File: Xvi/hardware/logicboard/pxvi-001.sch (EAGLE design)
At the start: 90 parts, among them J1 MKR, J4 QWIIC_RIGHT_ANGLE, J5 SPI, J6 QWIIC_RIGHT_ANGLE, J7 DIN5, K1 G5V1, Q1 60V/32A/35mΩ, Q10 60V/32A/35mΩ, Q11 60V/32A/35mΩ, Q12 60V/32A/35mΩ, Q13 60V/32A/35mΩ, Q14 60V/32A/35mΩ, Q15 60V/32A/35mΩ, Q16 60V/32A/35mΩ, Q2 60V/32A/35mΩ, Q3 60V/32A/35mΩ, Q4 60V/32A/35mΩ, Q5 60V/32A/35mΩ, Q6 60V/32A/35mΩ, Q7 60V/32A/35mΩ, Q8 60V/32A/35mΩ, Q9 60V/32A/35mΩ, T1 2SC1815, U1 DS18B20, X1 ADAFRUIT-PCA9685, X2 MKDSN1,5/2-5,08

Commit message: Wired.
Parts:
- added C25: 10n, resistor:C-EU025-024X044
- added D2: DIODE-1N4148, SparkFun-DiscreteSemi:DIODE-1N4148
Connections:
- net N$1: now also C25.2, D2.A
- net VCC: now also C25.1, D2.C
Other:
- moved on the sheet: K1, R2, R3
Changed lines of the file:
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@@
 <part name="SUPPLY62" library="supply2" library_urn="urn:adsk.eagle:library:372" deviceset="VCC" device=""/>
 <part name="P+20" library="supply1" library_urn="urn:adsk.eagle:library:371" deviceset="V+" device=""/>
+<part name="C25" library="resistor" library_urn="urn:adsk.eagle:library:348" deviceset="C-EU" device="025-024X044" package3d_urn="urn:adsk.eagle:package:23630/1" value="10n"/>
+<part name="D2" library="SparkFun-DiscreteSemi" library_urn="urn:adsk.eagle:library:514" deviceset="DIODE" device="-1N4148" package3d_urn="urn:adsk.eagle:package:38452/1" value=""/>
 </parts>
 <sheets>
@@
 <wire x1="360.68" y1="121.92" x2="304.8" y2="121.92" width="0.1524" layer="94" style="shortdash"/>
 <wire x1="218.44" y1="254" x2="218.44" y2="167.64" width="0.1524" layer="94" style="shortdash"/>
-<wire x1="218.44" y1="167.64" x2="335.28" y2="167.64" width="0.1524" layer="94" style="shortdash"/>
 <wire x1="335.28" y1="254" x2="218.44" y2="254" width="0.1524" layer="94" style="shortdash"/>
 </plain>
@@
 <attribute name="VALUE" x="327.66" y="157.48" size="1.778" layer="96"/>
 </instance>
-<instance part="K1" gate="1" x="340.36" y="165.1" smashed="yes">
-<attribute name="VALUE" x="341.63" y="168.021" size="1.778" layer="96"/>
-<attribute name="PART" x="341.63" y="170.18" size="1.778" layer="95"/>
+<instance part="K1" gate="1" x="340.36" y="170.18" smashed="yes">
+<attribute name="VALUE" x="341.63" y="173.101" size="1.778" layer="96"/>
+<attribute name="PART" x="341.63" y="175.26" size="1.778" layer="95"/>
 </instance>
 <instance part="K1" gate="2" x="358.14" y="162.56" smashed="yes">
@@
 </instance>
 <instance part="SUPPLY36" gate="GND" x="264.16" y="198.12" smashed="yes"/>
-<instance part="R2" gate="G$1" x="325.12" y="152.4" smashed="yes">
-<attribute name="NAME" x="325.12" y="154.94" size="1.778" layer="95" align="center"/>
-<attribute name="VALUE" x="330.2" y="154.94" size="1.778" layer="96" align="center"/>
-</instance>
-<instance part="R3" gate="G$1" x="332.74" y="139.7" smashed="yes" rot="R90">
-<attribute name="NAME" x="330.2" y="139.7" size="1.778" layer="95" rot="R90" align="center"/>
-<attribute name="VALUE" x="330.2" y="144.78" size="1.778" layer="96" rot="R90" align="center"/>
-</instance>
-<instance part="SUPPLY37" gate="GND" x="332.74" y="129.54" smashed="yes"/>
+<instance part="R2" gate="G$1" x="312.42" y="152.4" smashed="yes">
+<attribute name="NAME" x="312.42" y="154.94" size="1.778" layer="95" align="center"/>
+<attribute name="VALUE" x="317.5" y="154.94" size="1.778" layer="96" align="center"/>
+</instance>
+<instance part="R3" gate="G$1" x="320.04" y="142.24" smashed="yes" rot="R90">
+<attribute name="NAME" x="317.5" y="142.24" size="1.778" layer="95" rot="R90" align="center"/>
+<attribute name="VALUE" x="317.5" y="147.32" size="1.778" layer="96" rot="R90" align="center"/>
+</instance>
+<instance part="SUPPLY37" gate="GND" x="320.04" y="129.54" smashed="yes"/>
 <instance part="SUPPLY38" gate="G$1" x="373.38" y="182.88" smashed="yes">
 <attribute name="VALUE" x="373.38" y="187.96" size="1.778" layer="96" align="bottom-center"/>
@@
 <instance part="P+20" gate="1" x="274.32" y="236.22" smashed="yes">
 <attribute name="VALUE" x="274.32" y="238.76" size="1.778" layer="96"/>
+</instance>
+<instance part="C25" gate="G$1" x="325.12" y="170.18" smashed="yes">
+<attribute name="NAME" x="322.58" y="170.18" size="1.778" layer="95" align="bottom-center"/>
+<attribute name="VALUE" x="322.58" y="165.1" size="1.778" layer="96" align="bottom-center"/>
+</instance>
+<instance part="D2" gate="G$1" x="332.74" y="170.18" smashed="yes" rot="R90">
+<attribute name="NAME" x="337.82" y="170.18" size="1.778" layer="95" rot="R270" align="bottom-center"/>
+<attribute name="VALUE" x="334.772" y="167.64" size="1.778" layer="96" font="vector" rot="R90" align="top-left"/>
 </instance>
 </instances>
@@
 <segment>
 <pinref part="R3" gate="G$1" pin="1"/>
-<wire x1="332.74" y1="134.62" x2="332.74" y2="132.08" width="0.1524" layer="91"/>
+<wire x1="320.04" y1="137.16" x2="320.04" y2="132.08" width="0.1524" layer="91"/>
 <pinref part="SUPPLY37" gate="GND" pin="GND"/>
 </segment>
@@
 <pinref part="SUPPLY34" gate="G$1" pin="VCC"/>
 <pinref part="K1" gate="1" pin="1"/>
-<wire x1="340.36" y1="180.34" x2="340.36" y2="170.18" width="0.1524" layer="91"/>
+<wire x1="340.36" y1="180.34" x2="340.36" y2="177.8" width="0.1524" layer="91"/>
+<wire x1="340.36" y1="177.8" x2="340.36" y2="175.26" width="0.1524" layer="91"/>
+<wire x1="340.36" y1="177.8" x2="332.74" y2="177.8" width="0.1524" layer="91"/>
+<junction x="340.36" y="177.8"/>
+<pinref part="C25" gate="G$1" pin="1"/>
+<wire x1="332.74" y1="177.8" x2="325.12" y2="177.8" width="0.1524" layer="91"/>
+<wire x1="325.12" y1="177.8" x2="325.12" y2="172.72" width="0.1524" layer="91"/>
+<pinref part="D2" gate="G$1" pin="C"/>
+<wire x1="332.74" y1="172.72" x2="332.74" y2="177.8" width="0.1524" layer="91"/>
+<junction x="332.74" y="177.8"/>
 </segment>
 <segment>
@@
 <segment>
 <pinref part="R2" gate="G$1" pin="1"/>
-<wire x1="320.04" y1="152.4" x2="317.5" y2="152.4" width="0.1524" layer="91"/>
-<label x="317.5" y="152.4" size="0.8128" layer="95" rot="R180" xref="yes"/>
+<wire x1="307.34" y1="152.4" x2="304.8" y2="152.4" width="0.1524" layer="91"/>
+<label x="304.8" y="152.4" size="0.8128" layer="95" rot="R180" xref="yes"/>
 </segment>
 </net>
@@
 <pinref part="K1" gate="1" pin="2"/>
 <pinref part="T1" gate="G$1" pin="C"/>
-<wire x1="340.36" y1="160.02" x2="340.36" y2="157.48" width="0.1524" layer="91"/>
+<wire x1="340.36" y1="165.1" x2="340.36" y2="162.56" width="0.1524" layer="91"/>
+<pinref part="D2" gate="G$1" pin="A"/>
+<wire x1="340.36" y1="162.56" x2="340.36" y2="157.48" width="0.1524" layer="91"/>
+<wire x1="332.74" y1="167.64" x2="332.74" y2="162.56" width="0.1524" layer="91"/>
+<wire x1="332.74" y1="162.56" x2="340.36" y2="162.56" width="0.1524" layer="91"/>
+<junction x="340.36" y="162.56"/>
+<wire x1="332.74" y1="162.56" x2="325.12" y2="162.56" width="0.1524" layer="91"/>
+<junction x="332.74" y="162.56"/>
+<pinref part="C25" gate="G$1" pin="2"/>
+<wire x1="325.12" y1="162.56" x2="325.12" y2="165.1" width="0.1524" layer="91"/>
 </segment>
 </net>
@@
 <segment>
 <pinref part="T1" gate="G$1" pin="B"/>
-<wire x1="335.28" y1="152.4" x2="332.74" y2="152.4" width="0.1524" layer="91"/>
+<wire x1="335.28" y1="152.4" x2="320.04" y2="152.4" width="0.1524" layer="91"/>
 <pinref part="R2" gate="G$1" pin="2"/>
 <pinref part="R3" gate="G$1" pin="2"/>
-<wire x1="332.74" y1="152.4" x2="330.2" y2="152.4" width="0.1524" layer="91"/>
-<wire x1="332.74" y1="152.4" x2="332.74" y2="144.78" width="0.1524" layer="91"/>
-<junction x="332.74" y="152.4"/>
-</segment>
-</net>
+<wire x1="320.04" y1="152.4" x2="317.5" y2="152.4" width="0.1524" layer="91"/>
+<wire x1="320.04" y1="152.4" x2="320.04" y2="147.32" width="0.1524" layer="91"/>
+<junction x="320.04" y="152.4"/>
+</segment>
+</net>

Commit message: Wired.
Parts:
- removed J4, J6: QWIIC_RIGHT_ANGLE, SparkFun-Connectors:QWIIC_CONNECTORJS-1MM
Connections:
- net GND: no longer J4.1, J6.1
- net SCL: no longer J4.4, J6.4
- net SDA: no longer J4.3, J6.3
- net VCC: no longer J4.2, J6.2
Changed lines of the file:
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@@
 <part name="SUPPLY38" library="supply2" library_urn="urn:adsk.eagle:library:372" deviceset="VCC" device=""/>
 <part name="SUPPLY39" library="supply2" deviceset="GND" device=""/>
-<part name="J4" library="SparkFun-Connectors" library_urn="urn:adsk.eagle:library:513" deviceset="QWIIC_CONNECTOR" device="JS-1MM" package3d_urn="urn:adsk.eagle:package:41390393/1" value="QWIIC_RIGHT_ANGLE"/>
-<part name="J6" library="SparkFun-Connectors" library_urn="urn:adsk.eagle:library:513" deviceset="QWIIC_CONNECTOR" device="JS-1MM" package3d_urn="urn:adsk.eagle:package:41390393/1" value="QWIIC_RIGHT_ANGLE"/>
 <part name="SUPPLY40" library="supply2" library_urn="urn:adsk.eagle:library:372" deviceset="VCC" device=""/>
 <part name="SUPPLY41" library="supply2" deviceset="GND" device=""/>
@@
 </instance>
 <instance part="SUPPLY39" gate="GND" x="350.52" y="129.54" smashed="yes"/>
-<instance part="J4" gate="J1" x="215.9" y="139.7" smashed="yes">
-<attribute name="VALUE" x="210.82" y="134.366" size="1.778" layer="96" font="vector" align="top-left"/>
-<attribute name="NAME" x="210.82" y="147.574" size="1.778" layer="95" font="vector"/>
-</instance>
-<instance part="J6" gate="J1" x="215.9" y="116.84" smashed="yes">
-<attribute name="VALUE" x="210.82" y="111.506" size="1.778" layer="96" font="vector" align="top-left"/>
-<attribute name="NAME" x="210.82" y="124.714" size="1.778" layer="95" font="vector"/>
-</instance>
 <instance part="SUPPLY40" gate="G$1" x="246.38" y="149.86" smashed="yes">
 <attribute name="VALUE" x="246.38" y="154.94" size="1.778" layer="96" align="bottom-center"/>
@@
 </segment>
 <segment>
-<pinref part="J4" gate="J1" pin="1"/>
 <wire x1="223.52" y1="137.16" x2="233.68" y2="137.16" width="0.1524" layer="91"/>
 <wire x1="233.68" y1="137.16" x2="246.38" y2="137.16" width="0.1524" layer="91"/>
 <wire x1="246.38" y1="137.16" x2="246.38" y2="134.62" width="0.1524" layer="91"/>
-<pinref part="J6" gate="J1" pin="1"/>
 <wire x1="223.52" y1="114.3" x2="233.68" y2="114.3" width="0.1524" layer="91"/>
 <wire x1="233.68" y1="114.3" x2="233.68" y2="137.16" width="0.1524" layer="91"/>
@@
 </segment>
 <segment>
-<pinref part="J4" gate="J1" pin="2"/>
 <wire x1="223.52" y1="139.7" x2="231.14" y2="139.7" width="0.1524" layer="91"/>
-<pinref part="J6" gate="J1" pin="2"/>
 <wire x1="223.52" y1="116.84" x2="231.14" y2="116.84" width="0.1524" layer="91"/>
 <wire x1="231.14" y1="116.84" x2="231.14" y2="139.7" width="0.1524" layer="91"/>
@@
 </segment>
 <segment>
-<pinref part="J4" gate="J1" pin="3"/>
 <wire x1="223.52" y1="142.24" x2="228.6" y2="142.24" width="0.1524" layer="91"/>
-<pinref part="J6" gate="J1" pin="3"/>
 <wire x1="228.6" y1="142.24" x2="238.76" y2="142.24" width="0.1524" layer="91"/>
 <wire x1="228.6" y1="142.24" x2="228.6" y2="119.38" width="0.1524" layer="91"/>
@@
 </segment>
 <segment>
-<pinref part="J4" gate="J1" pin="4"/>
 <wire x1="223.52" y1="144.78" x2="226.06" y2="144.78" width="0.1524" layer="91"/>
-<pinref part="J6" gate="J1" pin="4"/>
 <wire x1="226.06" y1="144.78" x2="238.76" y2="144.78" width="0.1524" layer="91"/>
 <wire x1="223.52" y1="121.92" x2="226.06" y2="121.92" width="0.1524" layer="91"/>

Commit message: Re-routed.
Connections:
- net N$1 renamed VRLY
- net N$4 renamed FAN
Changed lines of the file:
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@@
 </segment>
 </net>
-<net name="N$1" class="0">
+<net name="VRLY" class="2">
 <segment>
 <pinref part="K1" gate="1" pin="2"/>
@@
 </segment>
 </net>
-<net name="N$4" class="0">
+<net name="FAN" class="2">
 <segment>
 <pinref part="X2" gate="-2" pin="KL"/>

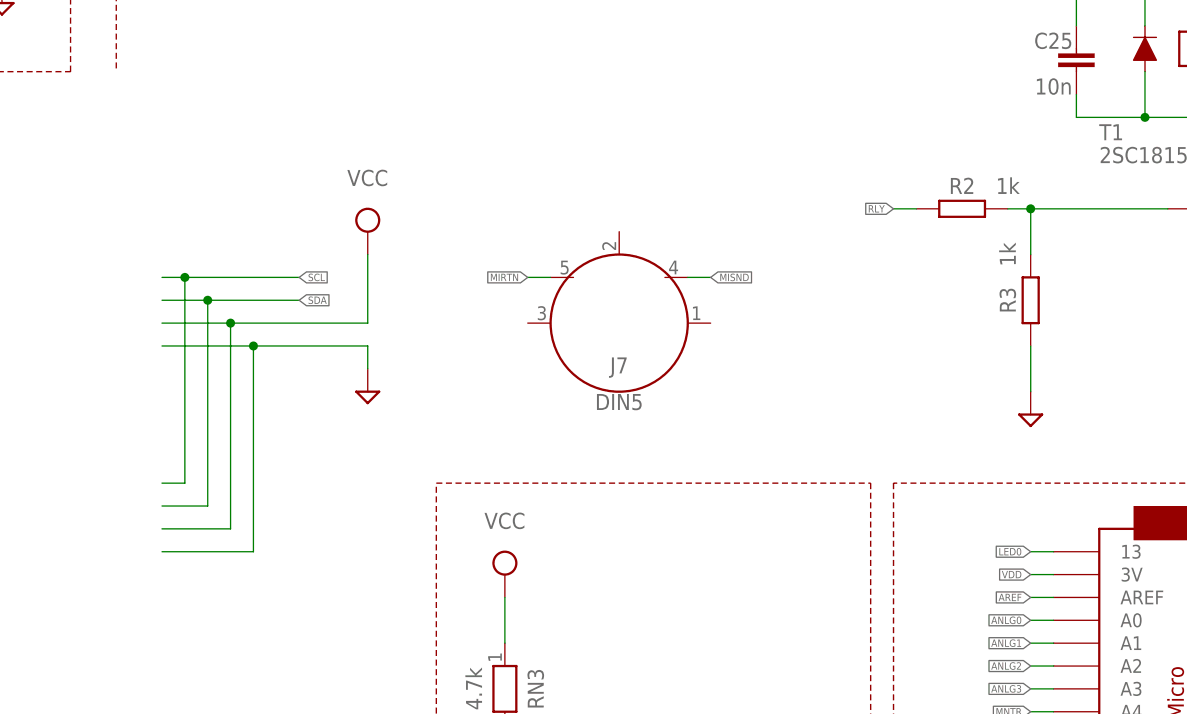
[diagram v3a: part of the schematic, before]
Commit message: GND pattern.
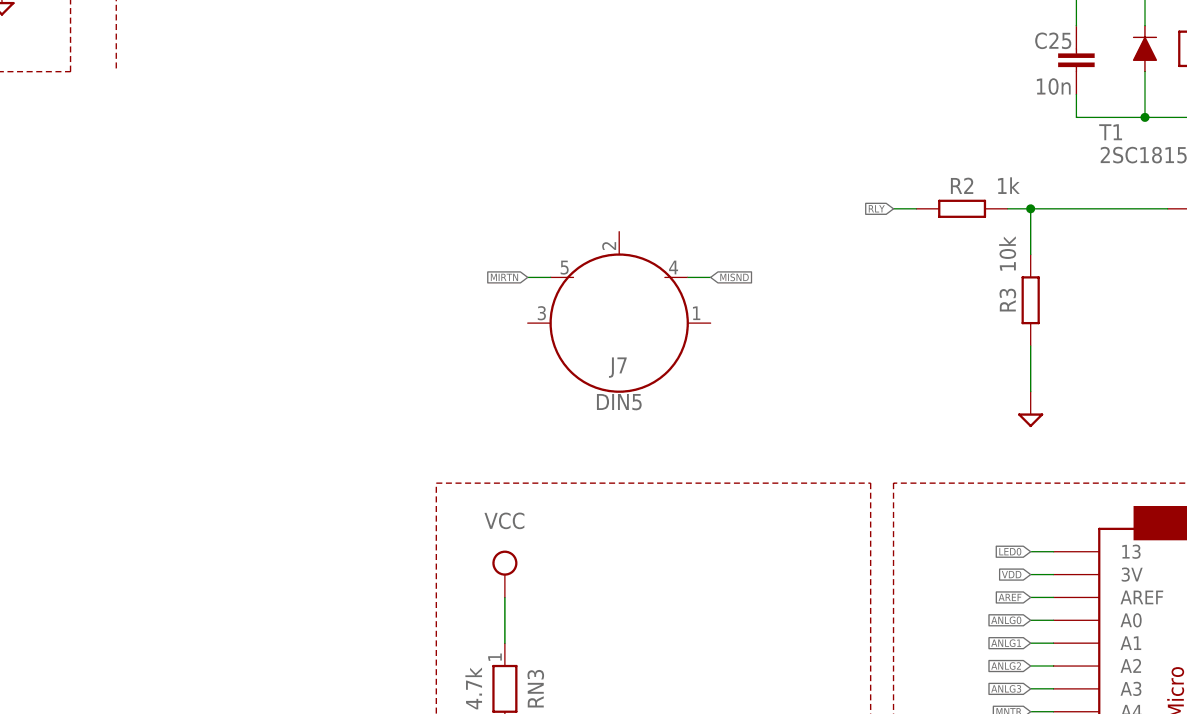
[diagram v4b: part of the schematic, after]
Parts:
- R3: value 1k -> 10k
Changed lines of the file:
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@@
 <part name="SUPPLY36" library="supply2" deviceset="GND" device=""/>
 <part name="R2" library="resistor" library_urn="urn:adsk.eagle:library:348" deviceset="R-EU_" device="0204/5" package3d_urn="urn:adsk.eagle:package:23488/1" value="1k"/>
-<part name="R3" library="resistor" library_urn="urn:adsk.eagle:library:348" deviceset="R-EU_" device="0204/5" package3d_urn="urn:adsk.eagle:package:23488/1" value="1k"/>
+<part name="R3" library="resistor" library_urn="urn:adsk.eagle:library:348" deviceset="R-EU_" device="0204/5" package3d_urn="urn:adsk.eagle:package:23488/1" value="10k"/>
 <part name="SUPPLY37" library="supply2" deviceset="GND" device=""/>
 <part name="SUPPLY38" library="supply2" library_urn="urn:adsk.eagle:library:372" deviceset="VCC" device=""/>
 <part name="SUPPLY39" library="supply2" deviceset="GND" device=""/>
-<part name="SUPPLY40" library="supply2" library_urn="urn:adsk.eagle:library:372" deviceset="VCC" device=""/>
-<part name="SUPPLY41" library="supply2" deviceset="GND" device=""/>
 <part name="J8" library="SparkFun-Connectors" library_urn="urn:adsk.eagle:library:513" deviceset="CONN_03" device="JST-PTH" package3d_urn="urn:adsk.eagle:package:38069/1"/>
 <part name="SUPPLY42" library="supply2" library_urn="urn:adsk.eagle:library:372" deviceset="VCC" device=""/>
@@
 </instance>
 <instance part="SUPPLY39" gate="GND" x="350.52" y="129.54" smashed="yes"/>
-<instance part="SUPPLY40" gate="G$1" x="246.38" y="149.86" smashed="yes">
-<attribute name="VALUE" x="246.38" y="154.94" size="1.778" layer="96" align="bottom-center"/>
-</instance>
-<instance part="SUPPLY41" gate="GND" x="246.38" y="132.08" smashed="yes"/>
 <instance part="J8" gate="J$1" x="190.5" y="182.88" smashed="yes">
 <attribute name="VALUE" x="187.96" y="175.514" size="1.778" layer="96" font="vector"/>
@@
 </segment>
 <segment>
-<wire x1="223.52" y1="137.16" x2="233.68" y2="137.16" width="0.1524" layer="91"/>
-<wire x1="233.68" y1="137.16" x2="246.38" y2="137.16" width="0.1524" layer="91"/>
-<wire x1="246.38" y1="137.16" x2="246.38" y2="134.62" width="0.1524" layer="91"/>
-<wire x1="223.52" y1="114.3" x2="233.68" y2="114.3" width="0.1524" layer="91"/>
-<wire x1="233.68" y1="114.3" x2="233.68" y2="137.16" width="0.1524" layer="91"/>
-<junction x="233.68" y="137.16"/>
-<pinref part="SUPPLY41" gate="GND" pin="GND"/>
-</segment>
-<segment>
 <pinref part="J8" gate="J$1" pin="1"/>
 <wire x1="198.12" y1="180.34" x2="205.74" y2="180.34" width="0.1524" layer="91"/>
@@
 </segment>
 <segment>
-<wire x1="223.52" y1="139.7" x2="231.14" y2="139.7" width="0.1524" layer="91"/>
-<wire x1="223.52" y1="116.84" x2="231.14" y2="116.84" width="0.1524" layer="91"/>
-<wire x1="231.14" y1="116.84" x2="231.14" y2="139.7" width="0.1524" layer="91"/>
-<junction x="231.14" y="139.7"/>
-<wire x1="231.14" y1="139.7" x2="246.38" y2="139.7" width="0.1524" layer="91"/>
-<wire x1="246.38" y1="139.7" x2="246.38" y2="147.32" width="0.1524" layer="91"/>
-<pinref part="SUPPLY40" gate="G$1" pin="VCC"/>
-</segment>
-<segment>
 <pinref part="J8" gate="J$1" pin="3"/>
 <wire x1="198.12" y1="185.42" x2="205.74" y2="185.42" width="0.1524" layer="91"/>
@@
 <label x="88.9" y="63.5" size="0.8128" layer="95" xref="yes"/>
 </segment>
-<segment>
-<wire x1="223.52" y1="142.24" x2="228.6" y2="142.24" width="0.1524" layer="91"/>
-<wire x1="228.6" y1="142.24" x2="238.76" y2="142.24" width="0.1524" layer="91"/>
-<wire x1="228.6" y1="142.24" x2="228.6" y2="119.38" width="0.1524" layer="91"/>
-<wire x1="228.6" y1="119.38" x2="223.52" y2="119.38" width="0.1524" layer="91"/>
-<junction x="228.6" y="142.24"/>
-<label x="238.76" y="142.24" size="0.8128" layer="95" xref="yes"/>
-</segment>
 </net>
 <net name="SCL" class="0">
@@
 <label x="88.9" y="60.96" size="0.8128" layer="95" xref="yes"/>
 </segment>
-<segment>
-<wire x1="223.52" y1="144.78" x2="226.06" y2="144.78" width="0.1524" layer="91"/>
-<wire x1="226.06" y1="144.78" x2="238.76" y2="144.78" width="0.1524" layer="91"/>
-<wire x1="223.52" y1="121.92" x2="226.06" y2="121.92" width="0.1524" layer="91"/>
-<wire x1="226.06" y1="121.92" x2="226.06" y2="144.78" width="0.1524" layer="91"/>
-<junction x="226.06" y="144.78"/>
-<label x="238.76" y="144.78" size="0.8128" layer="95" xref="yes"/>
-</segment>
-</net>
+</net>

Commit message: Silk.
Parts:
- removed C25: 10n, resistor:C-EU025-024X044
- removed R3: 10k, resistor:R-EU_0204/5
- added C102: (no value), rcl:C-EUC3216
- added R13: (no value), rcl:R-EU_R3216
- C9: value (none) -> 10n; device rcl:C-EUC3216 -> resistor:C-EU025-024X044
- R1: value 220 -> 1k
- R2: value 1k -> 10k
- R6: value (none) -> 220; device rcl:R-EU_R3216 -> resistor:R-EU_0204/5
- renumbered C10 to C103, C11 to C104, C12 to C105, C13 to C106, C14 to C107, C15 to C108, C16 to C109, C17 to C110, C18 to C111, C19 to C112, C20 to C113, C21 to C114, C22 to C115, C23 to C116, C24 to C100, DD1 to D101, DD10 to D110, DD11 to D111, DD12 to D112, DD13 to D113, DD14 to D114, DD15 to D115, DD16 to D116, DD2 to D102, DD3 to D103, DD4 to D104, DD5 to D105, DD6 to D106, DD7 to D107, DD8 to D108, DD9 to D109, DDUMMY to D100LED, J2 to J21, J3 to J22, J8 to J10, JP1 to JP0, SV1 to SV4, X1 to U2
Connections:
- net GND: now also R2.1; no longer R3.1
- net LD01: now also C102.2; no longer C9.2
- net MISND: now also R6.2; no longer R1.2
- net MISNDA: now also R6.1; no longer R1.1
- net N$2: now also R1.2; no longer R3.2
- net N$3: now also R13.1; no longer R6.1
- net RLY: now also R1.1; no longer R2.1
- net V+: now also C102.1, R13.2; no longer C9.1, R6.2
- net VCC: now also C9.1; no longer C25.1
- net VRLY: now also C9.2; no longer C25.2
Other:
- moved on the sheet: C9, R1, R2, R6
